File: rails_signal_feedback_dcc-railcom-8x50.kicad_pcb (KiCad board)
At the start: 2 copper layers, 8 parts, among them Q101 S8550, Q103 S8050, Q104 S8550

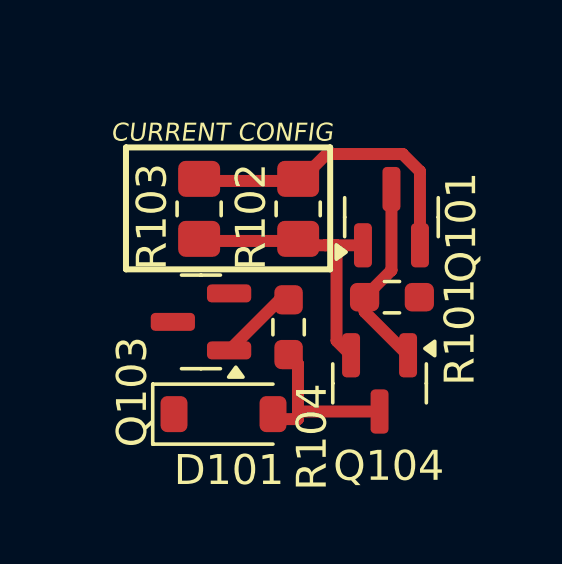
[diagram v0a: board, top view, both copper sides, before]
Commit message: Chg - Clearer PCB layout
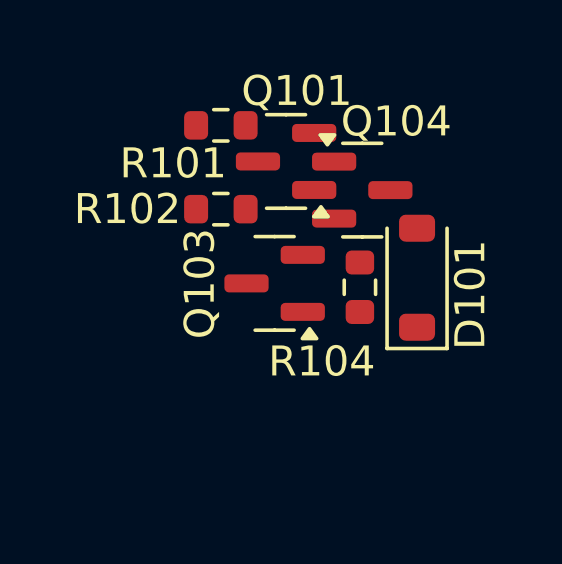
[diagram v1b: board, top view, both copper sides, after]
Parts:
- removed R103: 1M, Resistor_SMD:R_0805_2012Metric_Pad1.20x1.40mm_HandSolder
- R101, R104: footprint Resistor_SMD:R_0603_1608Metric_Pad0.98x0.95mm_HandSolder -> Resistor_SMD:R_0603_1608Metric
- R102: footprint Resistor_SMD:R_0805_2012Metric_Pad1.20x1.40mm_HandSolder -> Resistor_SMD:R_0603_1608Metric
- moved R101 8.08 mm to (149.2, 57.0), turned to 180 degrees
- moved D101 7.89 mm to (155.7, 62.1), turned to 90 degrees
- moved Q104 6.47 mm to (153.9, 59.2), turned to 0 degrees
- moved Q101 3.97 mm to (151.3, 58.2), turned to 180 degrees
- moved Q103 2.77 mm to (151.0, 62.3)
- moved R104 2.72 mm to (153.8, 62.4), turned to -90 degrees
- moved R102 2.58 mm to (149.2, 59.8), turned to 180 degrees
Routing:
- net /+3V3: track 10.4 -> 0.00 mm
- net /RC_CURR: track 9.34 -> 0.00 mm
- net /RC_DATA_IN: track 6.51 -> 0.00 mm
- net /RC_SIGNAL: track 5.82 -> 0.00 mm
- net Net-(Q103-B): track 2.68 -> 0.00 mm
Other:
- board text removed: "CURRENT CONFIG"
